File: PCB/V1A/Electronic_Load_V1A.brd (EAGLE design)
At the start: 100 x 100 mm, 227 parts, among them IC101 LM50, IC102 LM50, IC301 7805T, IC302 7805T, Q101 SIRC10DP, Q102 SIRC10DP, Q103 BC817-16SMD, Q104 BC817-16SMD, Q105 BC807-16SMD, Q106 SIRC10DP, Q107 IXTK102N65X2R+, Q108 SIRC10DP, Q109 SIRC10DP, Q110 SIRC10DP, Q111 IXTK102N65X2R+, Q601 BC807-16SMD, Q602 BC807-16SMD, Q603 BC807-16SMD, Q604 BC807-16SMD, Q605 BC807-16SMD, Q606 BC807-16SMD, Q607 BC807-16SMD, Q608 BC807-16SMD, Q609 BC807-16SMD, Q610 BC807-16SMD, Q611 BC807-16SMD, Q612 BC807-16SMD, U101 AD420, U102 AD420, U103 LT1014I, U104 LTC1865L, U201 AD620, U202 AD620, U203 AD620, U204 AD620, U205 AD620, U206 LTC1865L, U207 LTC1865L, U208 LTC1865L, U301 MAX743, U302 LT1014, U601 HCPL-063N, U602 HCPL-063N, U603 HCPL-063N, U604 HCPL-063N, U605 HCPL-063N, U606 HCPL-063N

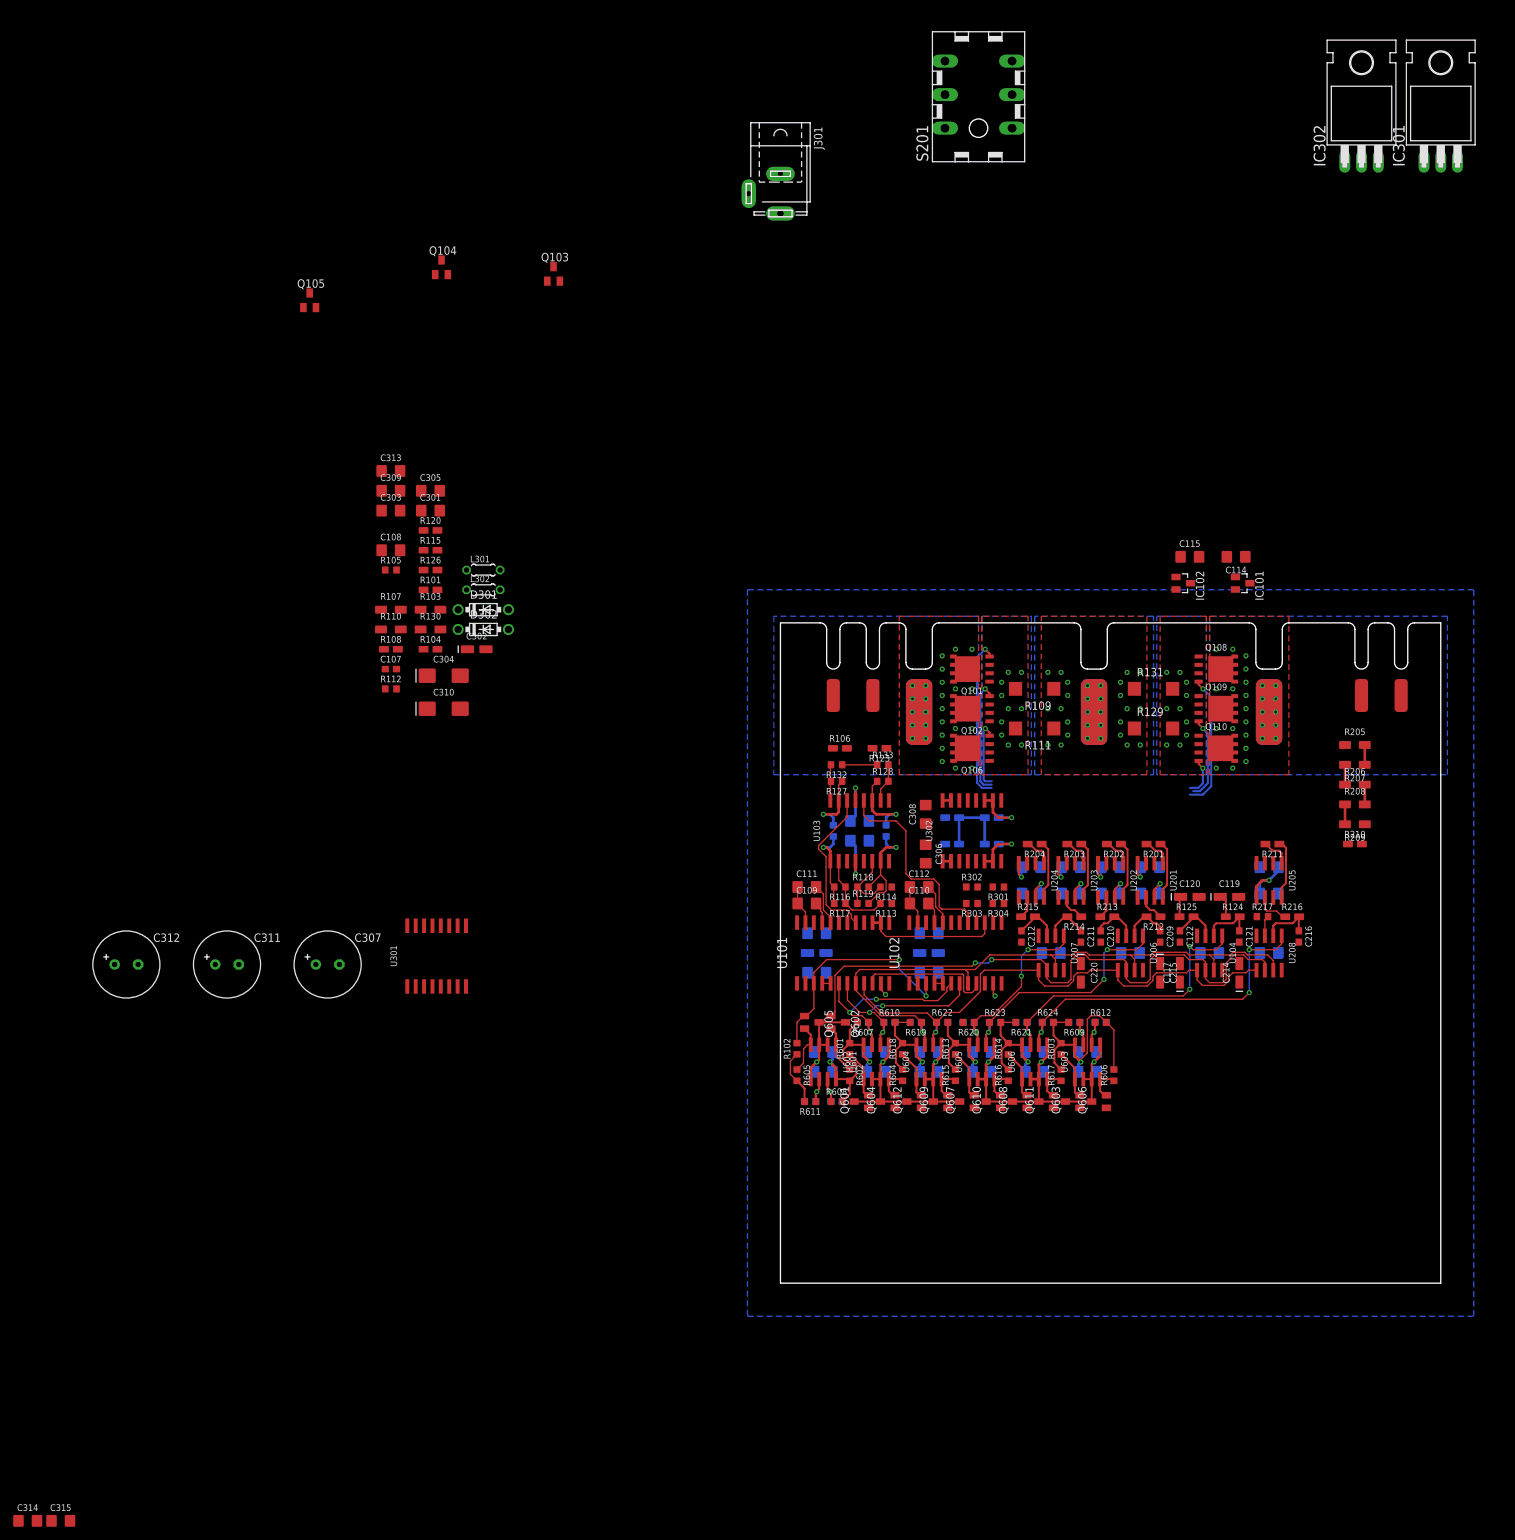
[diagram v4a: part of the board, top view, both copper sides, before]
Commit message: Board layout, added remote sense input protection
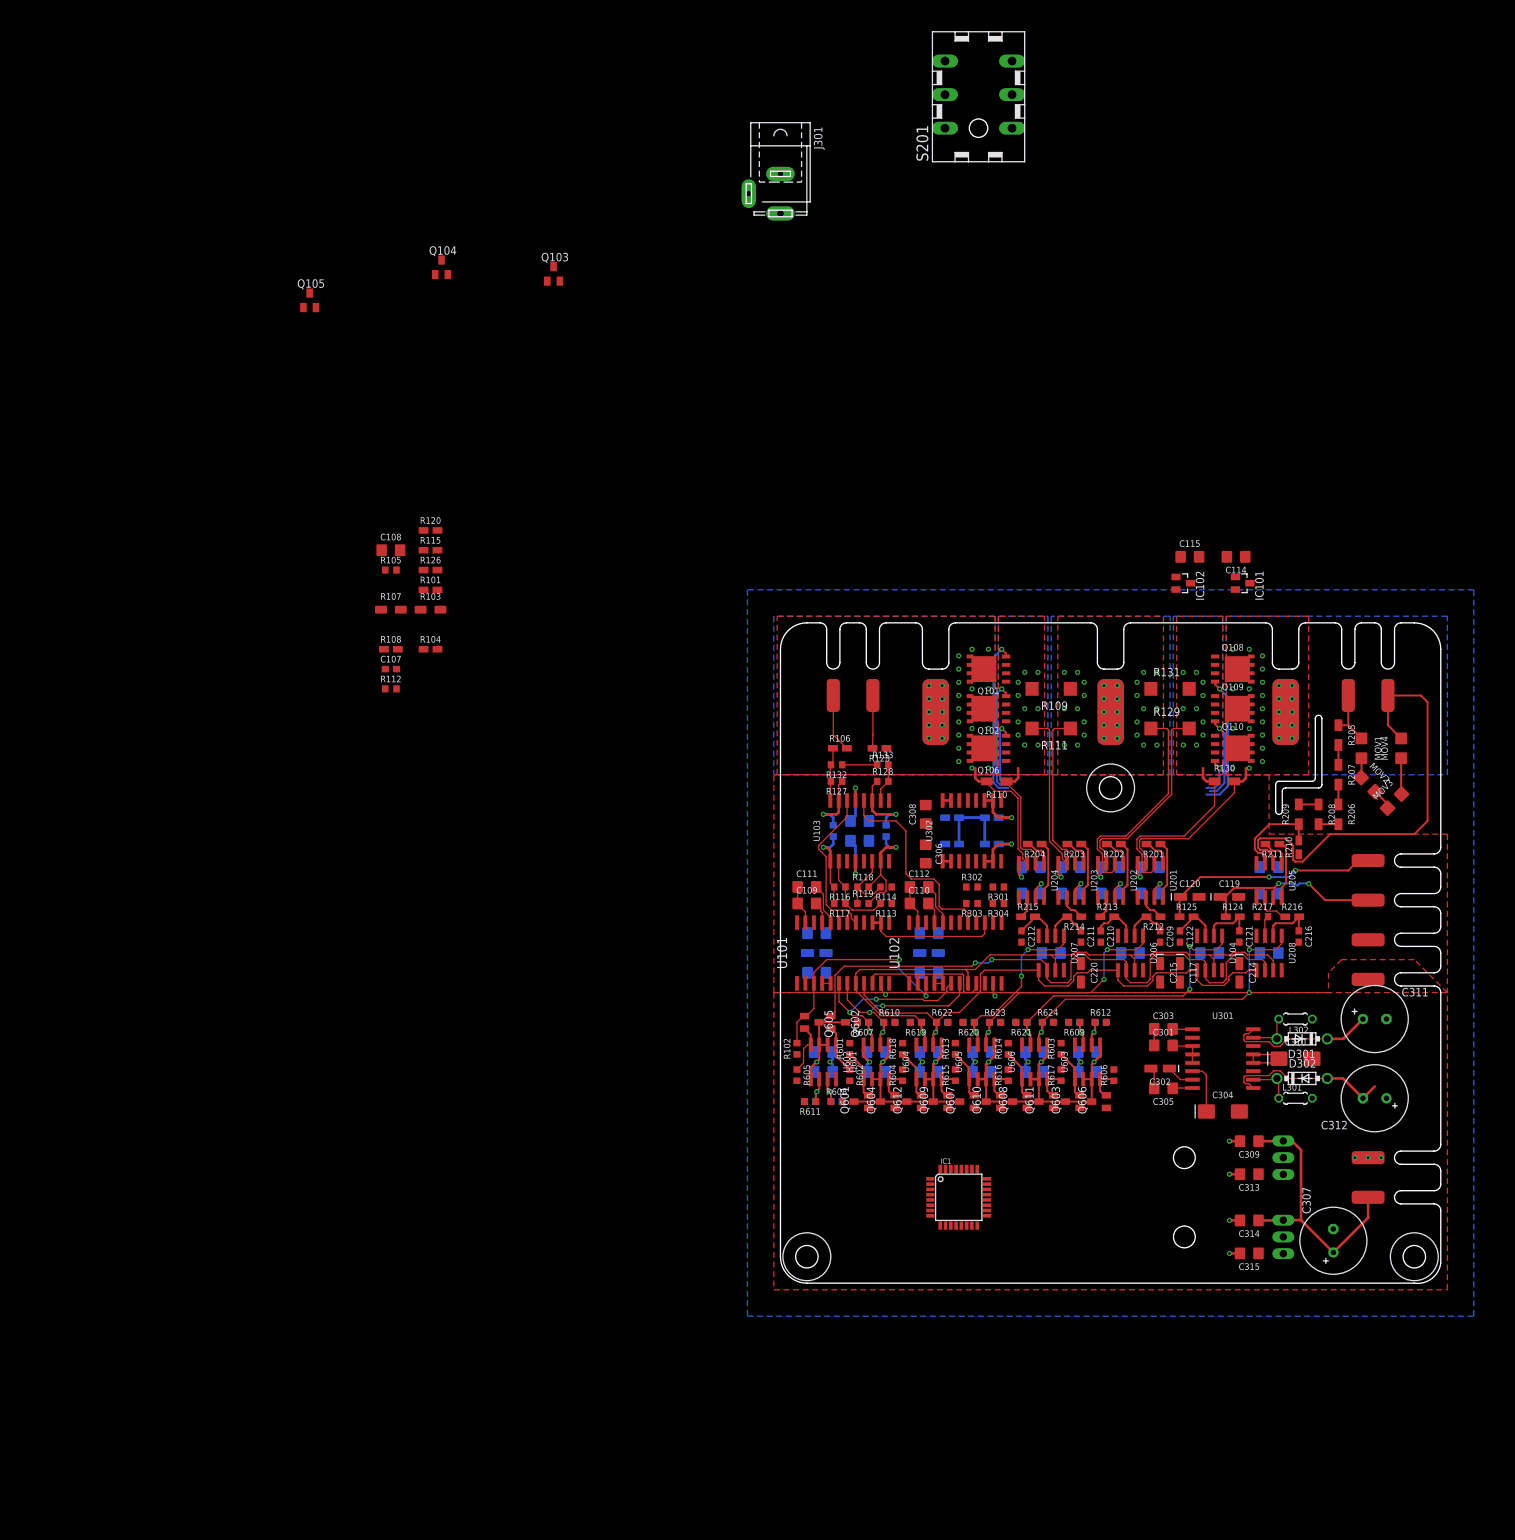
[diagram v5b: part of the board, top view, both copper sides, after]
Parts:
- added IC1: MEGA8-AI, atmel:TQFP32-08
- added MOV1, MOV2, MOV3, MOV4: 180V, passives:R3225W
- added PAD4: 12V, pads:PAD-5X2
- added PAD5, PAD9: GND, pads:PAD-5X2
- added PAD6: T1, pads:PAD-5X2
- added PAD7: T2, pads:PAD-5X2
- added PAD8: 5V, pads:PAD-5X2
- added U$1, U$2, U$3: (no value), mechanical:M3
- moved C314 190.5 mm to (71.0, 9.50), turned to 180 degrees
- moved C312 190.1 mm to (90.0, 28.0), turned to 180 degrees
- moved C315 184.5 mm to (71.0, 4.50), turned to 180 degrees
- moved IC302 174.4 mm to (66.0, 7.00), flipped to the bottom, turned to 270 degrees
- moved C311 174.0 mm to (90.0, 40.0)
- moved C313 168.1 mm to (71.0, 16.5), turned to 180 degrees
- moved IC301 164.6 mm to (66.0, 19.0), flipped to the bottom, turned to 270 degrees
- moved C309 163.1 mm to (71.0, 21.5), turned to 180 degrees
- moved C307 158.0 mm to (83.7, 6.42), turned to 90 degrees
- moved L301 146.7 mm to (78.0, 28.0)
- moved C305 143.2 mm to (58.0, 29.5), turned to 180 degrees
- moved D302 141.4 mm to (79.0, 31.0)
- moved C303 140.9 mm to (58.0, 38.5)
- moved D301 140.0 mm to (79.0, 37.0), turned to 180 degrees
- moved C310 139.5 mm to (78.0, 34.0)
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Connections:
- removed net N$42: C309.2, C313.2, IC301.2
- removed net N$44: C314.2, C315.2, IC302.2
- new net AVCC: IC1.18
- new net N$1: MOV1.2, MOV2.1
- new net N$2: MOV2.2, MOV3.1
- new net N$36: MOV3.2, MOV4.1
- new net VCC: IC1.4, IC1.6
- net +12V: now also PAD4.1
- net +5V: now also PAD8.1
- net CSENSE1_H: now also U203.3, U204.2; no longer U201.3, U203.2
- net CSENSE1_L: now also U204.3; no longer U203.3
- net CSENSE2_H: now also U201.2; no longer U204.2
- net CSENSE2_L: now also U201.3; no longer U204.3
- net GND: now also C309.2, C313.2, C314.2, C315.2, IC1.21, IC1.3, IC1.5, IC301.2, IC302.2, PAD5.1, PAD9.1; no longer U201.2, U202.2
- net T1_OUT: now also PAD6.1
- net T2_OUT: now also PAD7.1
- net UUT-: now also U202.2, U203.2
- net VSENSE+: now also MOV1.1
- net VSENSE-: now also MOV4.2
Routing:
- net +5V: track 134.0 -> 40.7 mm
- net VSENSE-: track 0.00 -> 67.8 mm
- net CSENSE2_H: track 0.00 -> 59.5 mm
- net UUT-: track 0.00 -> 59.0 mm
- net CSENSE1_H: track 0.00 -> 42.4 mm
- net +12V: track 11.8 -> 53.4 mm
- net T2_OUT: track 3.06 -> 33.7 mm, vias 0 -> 2
- net CSENSE2_L: track 0.00 -> 26.4 mm
- net -15V: track 22.5 -> 47.7 mm
- net T1_OUT: track 3.59 -> 28.1 mm, vias 0 -> 2
- net +15V: track 23.2 -> 45.9 mm
- net CSENSE1_L: track 0.00 -> 19.8 mm
- net N$29: track 0.00 -> 14.6 mm
- net GATE1: track 0.00 -> 8.85 mm
- net VSENSE+: track 0.00 -> 8.83 mm
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- added copper zone on layer 1, net +3V3
- added copper zone on layer 1, net +5V
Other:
- outline, holes or cut-outs redrawn
- board text added: "+12V In"
- board text added: "+5V Out"
- board text added: "Gate 1"
- board text added: "Gate 2"
- board text added: "Source 1"
- board text added: "Source 2"
- board text added: "Temp 1"
- board text added: "Temp 2"
- board text added: "UUT-"
- board text added: "Voltage sense"
